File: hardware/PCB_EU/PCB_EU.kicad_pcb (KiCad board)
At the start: 4 copper layers, 100 x 100 mm, 200 parts, among them J101 24 V IN, J201 UART 3V3, J301 MEM2061 SPI, J401 SHT4x XH2.54-4P-90, J403 FLOAT / GND, J411 FAN1 2510-4P, J421 FAN2 2510-4P, J501 LED1 + / GND, J601 LED2 + / GND, J602 BAR2 + / GND, J701 PTC + / RETURN, J702 PUMP + / RETURN, Q102 IRF1010ESPBF, Q411 FAN1 AO3422, Q421 FAN2 AO3422, Q501 TK22E10N1, Q601 TK22E10N1, Q701 BC847B-DIO, Q702 BC857B, Q703 IRF1010ESPBF, Q704 AO3422, SW201 RESET, SW202 BOOT, U101 L7987 3A, U102 INA226, U201 AP63203WU-7, U202 ESP32-WROOM-32E-N4, U301 MCP7940N-I/SN, U401 USBLC6-2SC6, U402 USBLC6-2SC6, U501 LM3429MH/NOPB, U601 LM3429MH/NOPB, U802 LM2903D-ST, Y301 32.768k CL7p

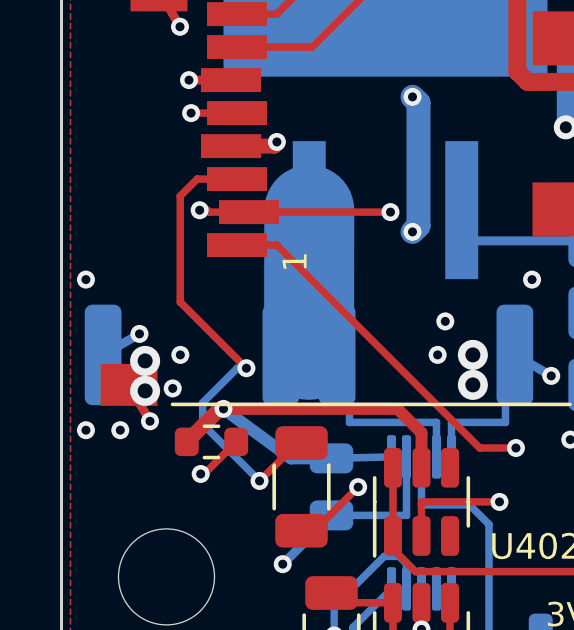
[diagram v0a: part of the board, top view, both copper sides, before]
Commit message: PCB_EU: write the board as the output of the documented rebuild
The PCB committed with #79 differed from build_board -> route_power ->
route_board (saved sessions) -> silkscreen.py: it lacked two GND vias
(1.96, 75.09) and (2.66, 76.327) and a 0.3 mm B.Cu stub, and kept the old
"HS guide holes" label. Write the rebuilt board (1446 tracks / 344 vias,
two rebuilds identical) and refresh review/* and the counts in the docs.
ERC, DRC (0 / 0 parity / 0 unconnected), silkscreen, stackup and DC power
screening pass; no design change.

Co-Authored-By: Claude Sonnet 5.5 <noreply@anthropic.com>
Claude-Session: https://claude.ai/code/session_01AxccZX6Cb4FnRKJMrFYMSX
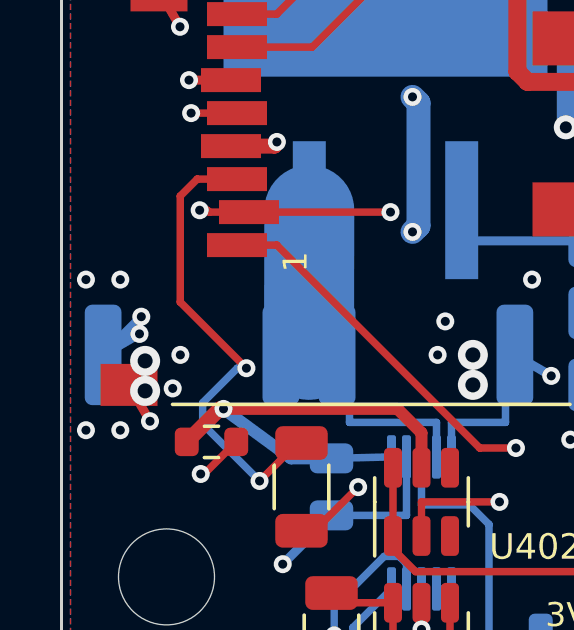
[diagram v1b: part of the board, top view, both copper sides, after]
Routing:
- net GND: track 198.3 -> 200.1 mm, vias 142 -> 144
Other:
- board text added: "Glue-mounted HS1 / physical fit and thermal NOT qualified"
- board text removed: "HS guide holes / thermal / routing NOT qualified"
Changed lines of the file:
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@@
 		(layer "Edge.Cuts")
 	)
-	(gr_text "HS guide holes / thermal / routing NOT qualified"
+	(gr_text "Glue-mounted HS1 / physical fit and thermal NOT qualified"
 		(at 50 -14.5 0)
 		(layer "Dwgs.User")
@@
 	)
 	(via
+		(at 1.96 75.09)
+		(size 0.6)
+		(drill 0.3)
+		(layers "F.Cu" "B.Cu")
+		(net "GND")
+	)
+	(via
 		(at 44.51 88.54)
 		(size 0.6)
@@
 	(via
 		(at 78.916 88.034)
+		(size 0.6)
+		(drill 0.3)
+		(layers "F.Cu" "B.Cu")
+		(net "GND")
+	)
+	(via
+		(at 2.66 76.327)
 		(size 0.6)
 		(drill 0.3)
@@
 		(layer "B.Cu")
 		(net "GND")
+	)
+	(segment
+		(start 1.3875 77.6)
+		(end 2.66 76.327)
+		(width 0.3)
+		(layer "B.Cu")
+		(net "GND")
